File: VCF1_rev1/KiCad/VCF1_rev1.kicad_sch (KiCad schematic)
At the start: 0 parts

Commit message: A lot of work especially on VCF2. Doc updated. Schematics a bit in a flux due to major restructuring.
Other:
- sheet CEM3350_1 renamed VCF_1_4
- sheet CEM3350_2 renamed VCF_2
- added sheet Power (Power.kicad_sch)
- added sheet VCF_3 (VCF_3.kicad_sch)
- sheet VCF_1_4: file CEM3350.kicad_sch -> VCF_1_4.kicad_sch
- sheet VCF_2: file CEM3350.kicad_sch -> VCF_2.kicad_sch
- sheet VCF_2 ports: added VCF2_VCA_CV, VCF2_out; removed VCF1_BPHP_in, VCF1_HP_out, VCF1_LPBP_out, VCF1_LP_in, VCF1_frequency_sum, VCF1_resonance_sum, VCF2_HP_out, VCF2_LPBP_out, VCF_Iref

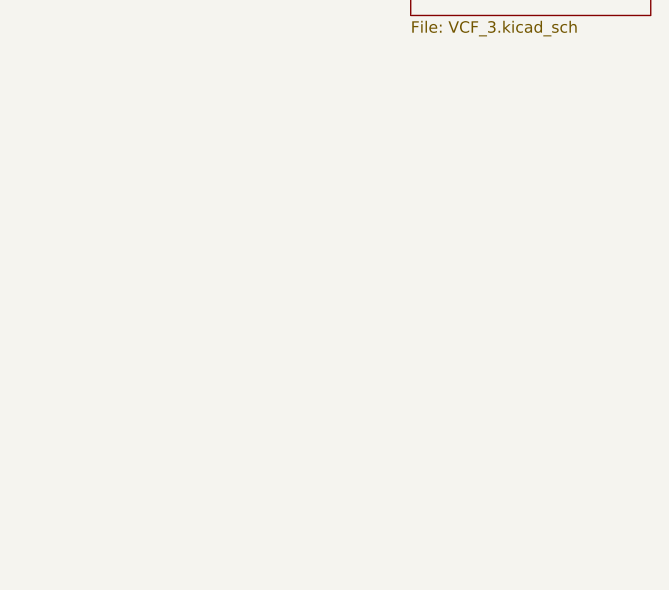
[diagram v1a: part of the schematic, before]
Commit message: Added VCA (with a quirk) and also drew a new symbol for 74HC4053 because the standard one annoyed me.
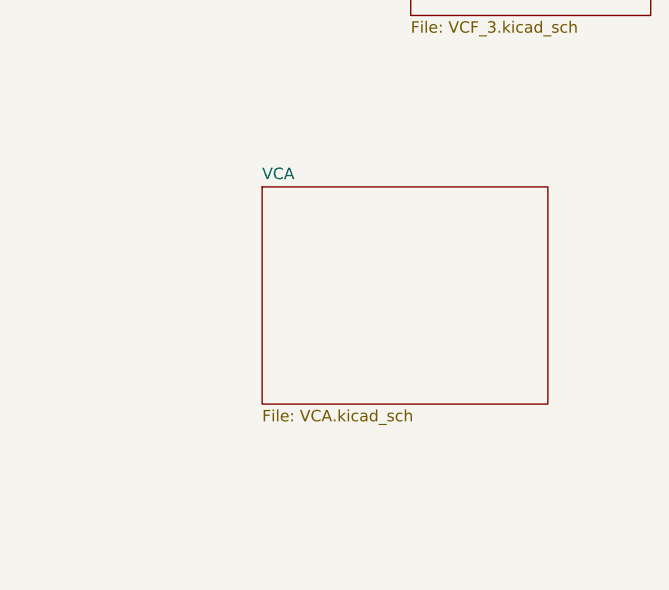
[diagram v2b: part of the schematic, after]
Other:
- added sheet VCA (VCA.kicad_sch)

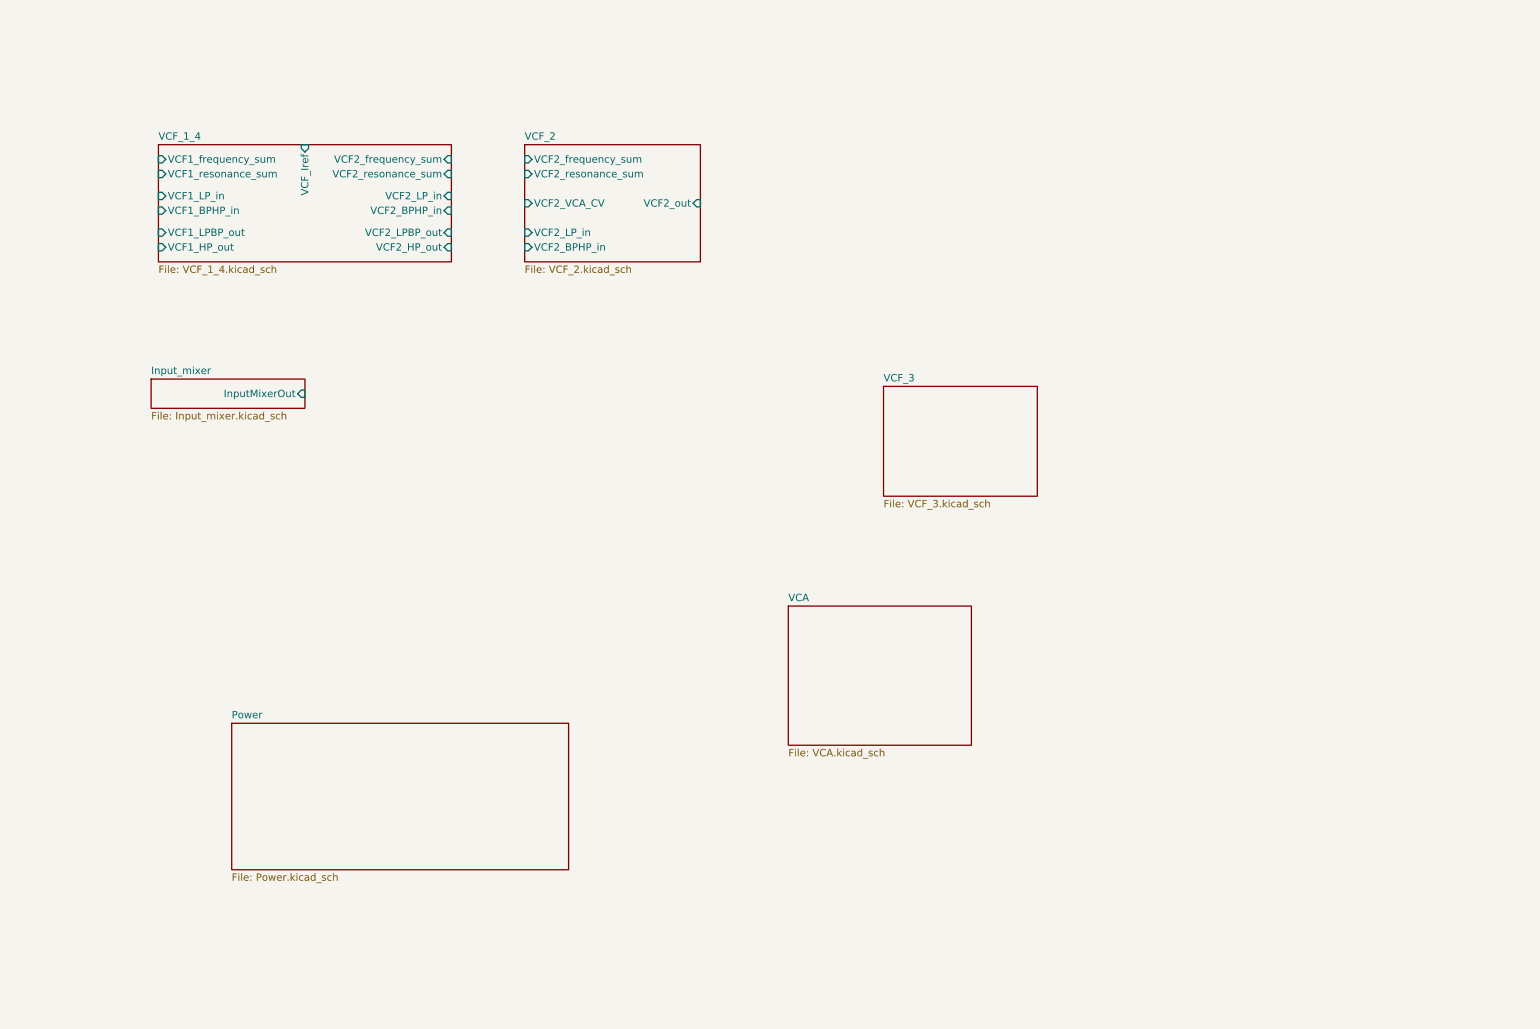
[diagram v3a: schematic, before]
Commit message: The filter blocks are more or less done, page order has gotten more sane for easier reading.
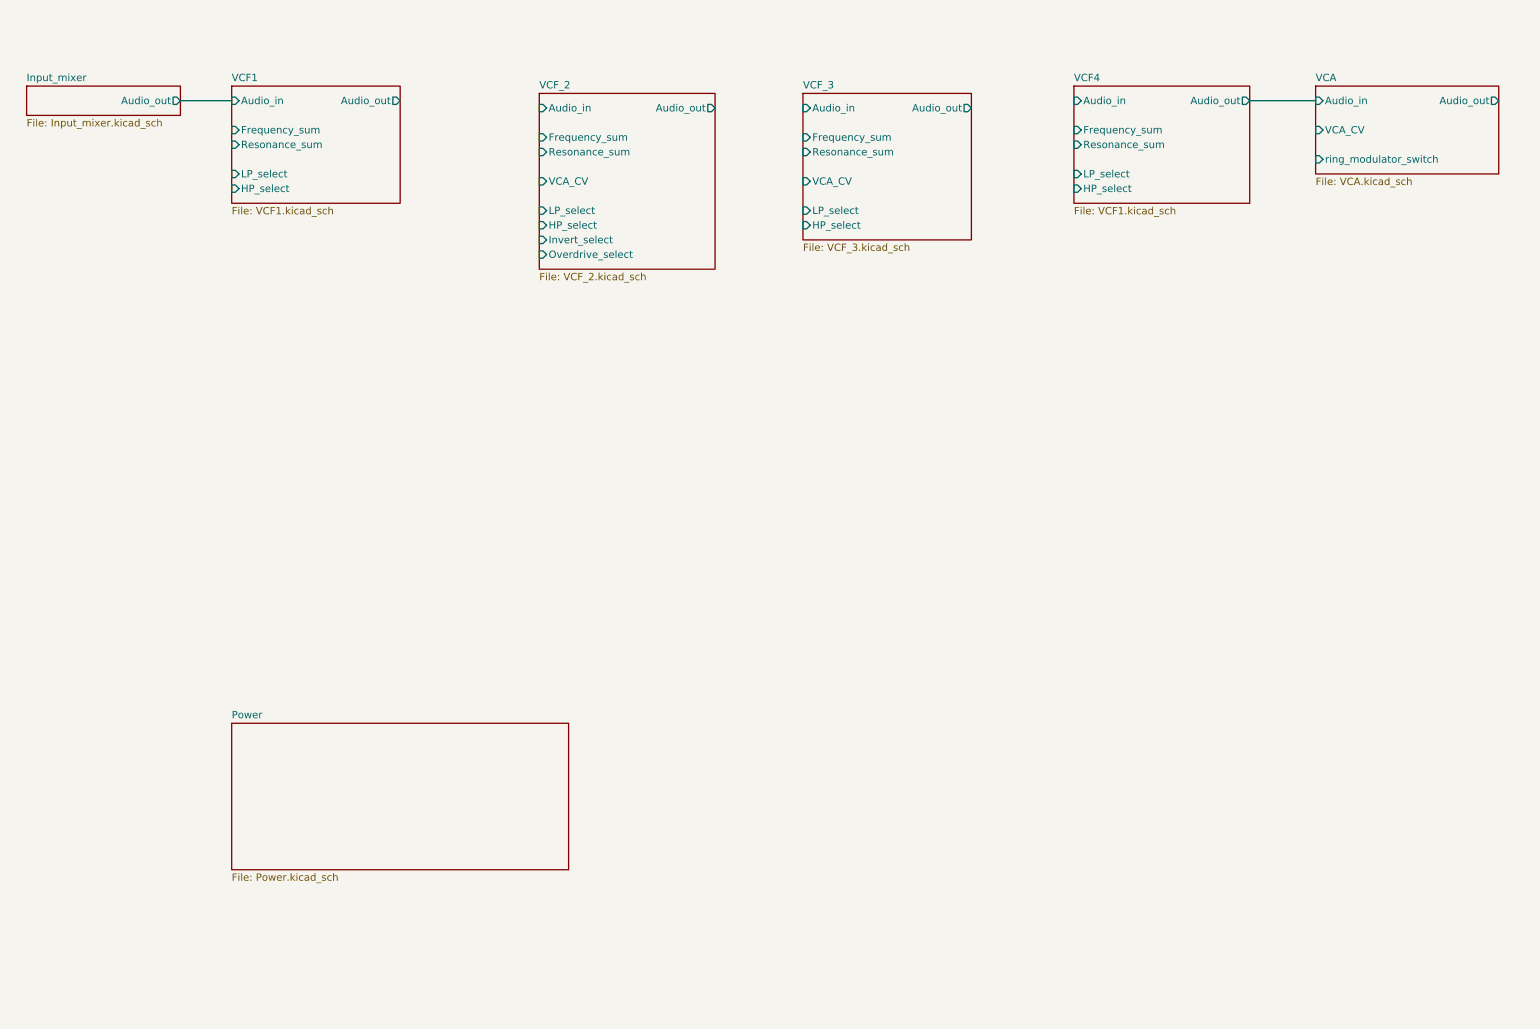
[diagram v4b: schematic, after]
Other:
- removed sheet VCF_1_4
- added sheet VCF1 (VCF1.kicad_sch)
- added sheet VCF4 (VCF1.kicad_sch)
- sheet Input_mixer ports: added Audio_out; removed InputMixerOut
- sheet VCA ports: added Audio_in, Audio_out, VCA_CV, ring_modulator_switch; removed none
- sheet VCF_2 ports: added Audio_in, Audio_out, Frequency_sum, HP_select, Invert_select, LP_select, Overdrive_select, Resonance_sum, VCA_CV; removed VCF2_BPHP_in, VCF2_LP_in, VCF2_VCA_CV, VCF2_frequency_sum, VCF2_out, VCF2_resonance_sum
- sheet VCF_3 ports: added Audio_in, Audio_out, Frequency_sum, HP_select, LP_select, Resonance_sum, VCA_CV; removed none

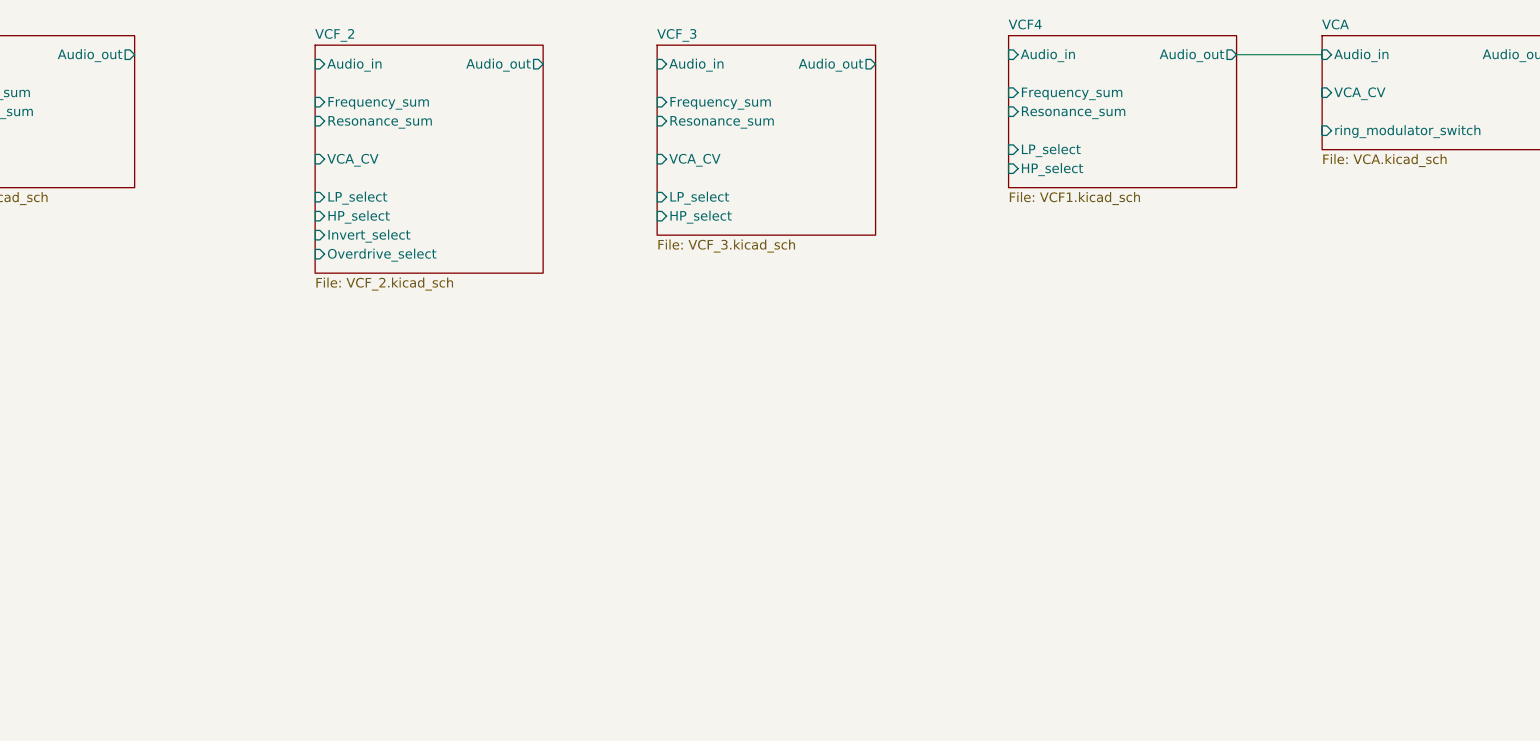
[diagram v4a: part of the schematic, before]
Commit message: Added the MUX. The signal path is now more or less complete!
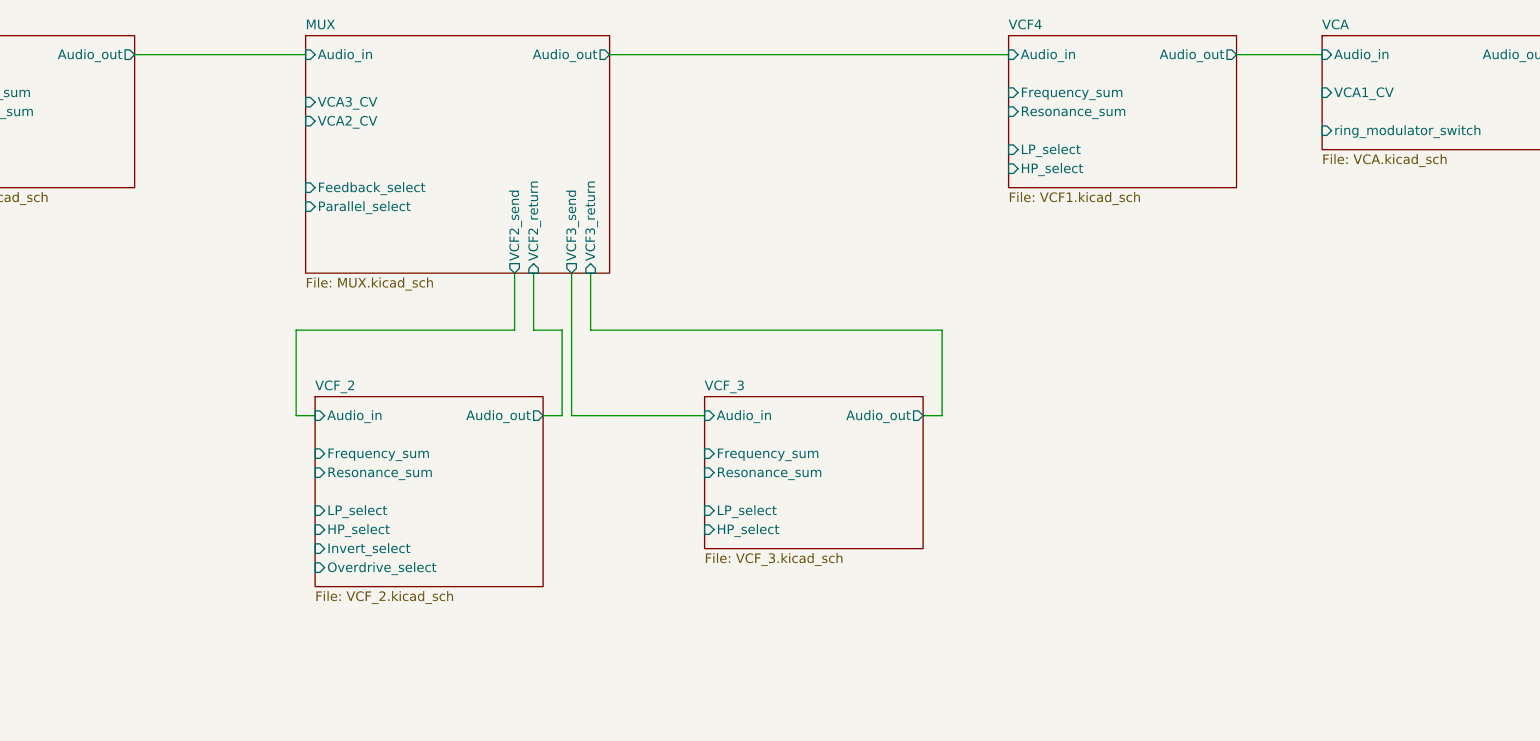
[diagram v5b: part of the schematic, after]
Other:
- added sheet MUX (MUX.kicad_sch)
- sheet VCA ports: added VCA1_CV; removed VCA_CV
- sheet VCF_2 ports: added none; removed VCA_CV
- sheet VCF_3 ports: added none; removed VCA_CV

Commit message: Lot of work on panel etc.
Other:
- added sheet Audiopanel (Audiopanel.kicad_sch)
- added sheet Controlpanel (Controlpanel.kicad_sch)

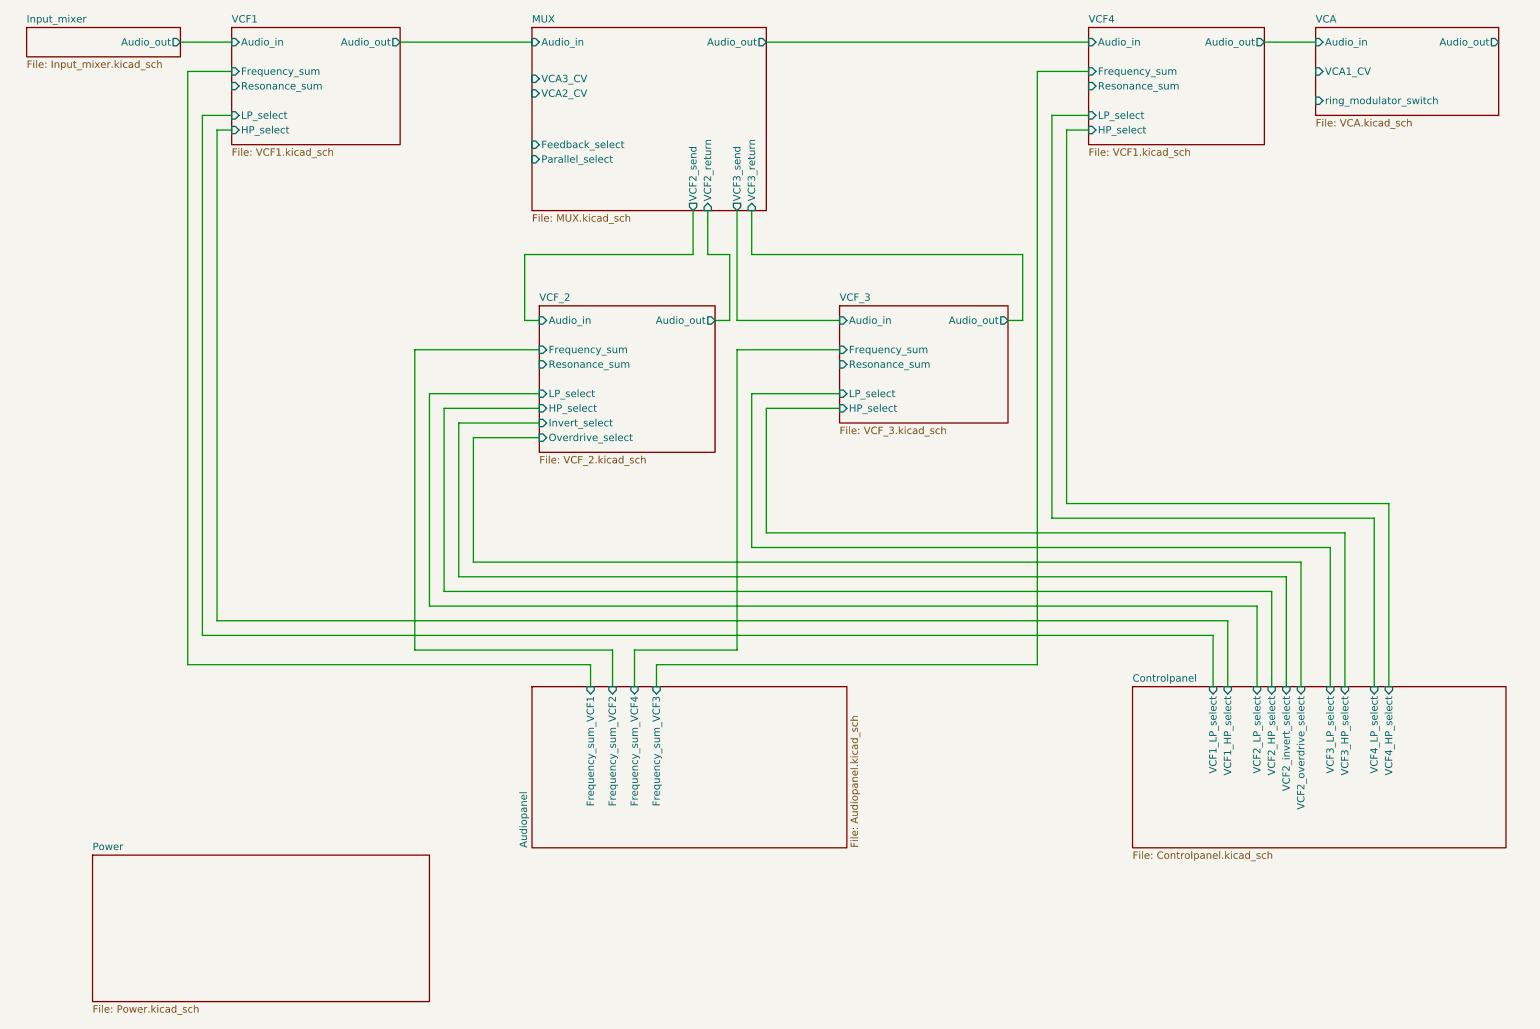
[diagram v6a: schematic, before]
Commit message: Cleaned up the first page with the overview and tried to make it a bit more readable.
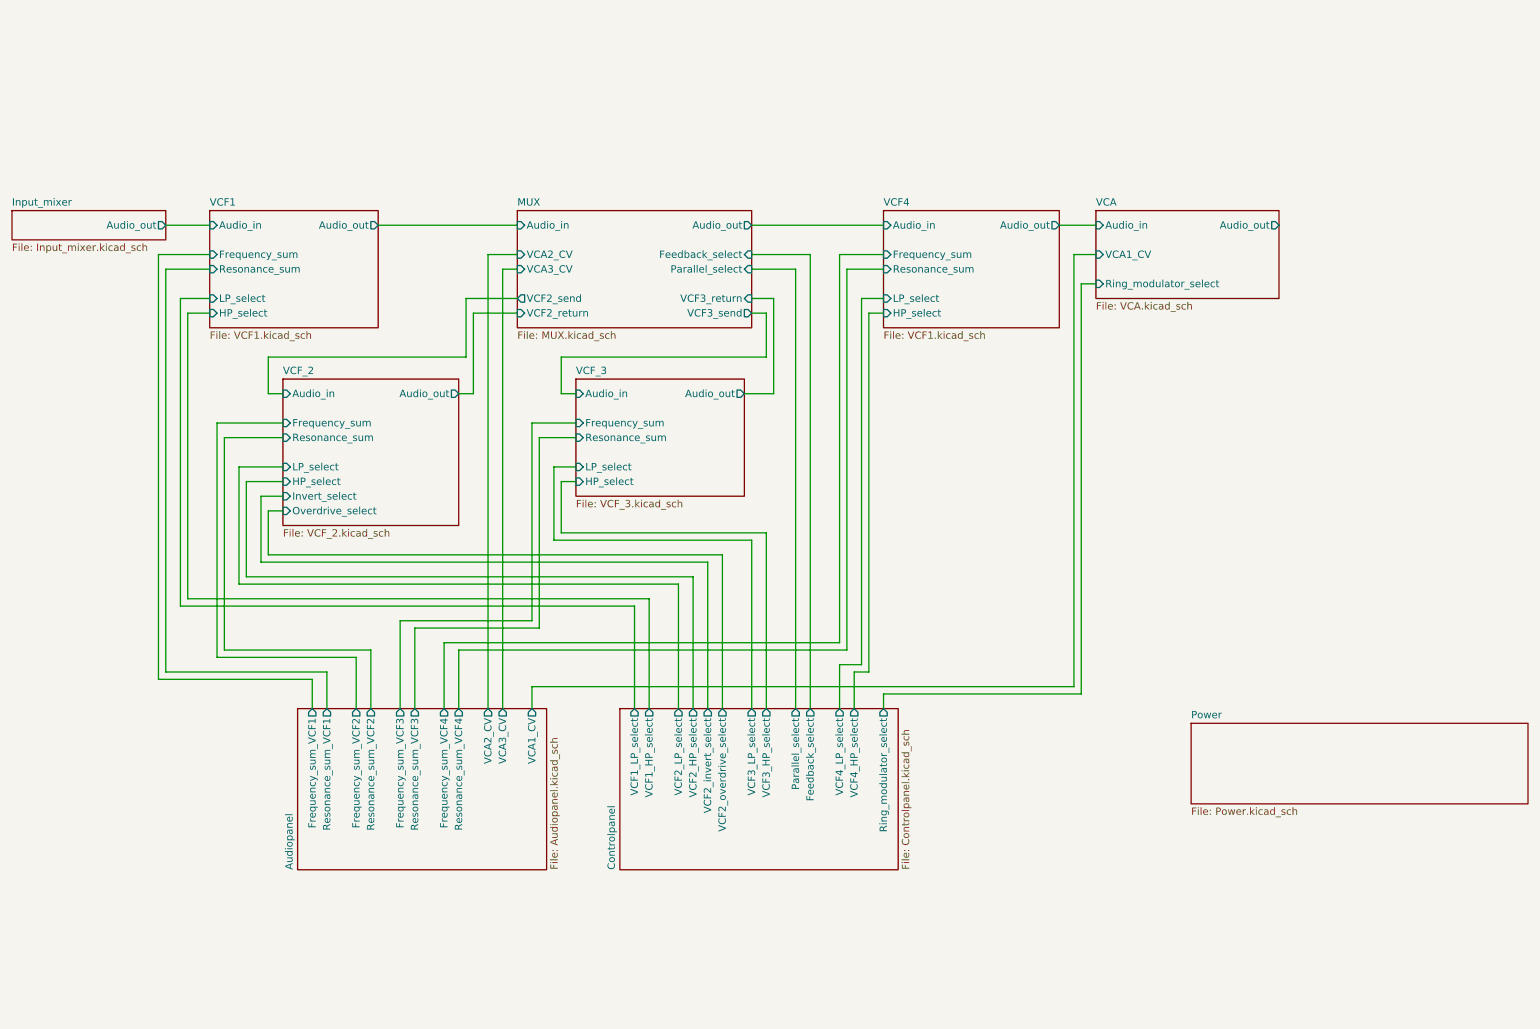
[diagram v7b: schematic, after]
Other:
- sheet Audiopanel ports: added Resonance_sum_VCF1, Resonance_sum_VCF2, Resonance_sum_VCF3, Resonance_sum_VCF4, VCA1_CV, VCA2_CV, VCA3_CV; removed none
- sheet Controlpanel ports: added Feedback_select, Parallel_select, Ring_modulator_select; removed none
- sheet VCA ports: added Ring_modulator_select; removed ring_modulator_switch
